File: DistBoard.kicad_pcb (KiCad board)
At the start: 2 copper layers, 63.6 x 50.8 mm, 21 parts, among them J1 22-27-2021, J2 SSM-103-L-SV, J3 SSM-103-L-SV, J4 SSM-103-L-SV, J5 SSM-103-L-SV, U1 TLE2426CDR

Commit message: Import board settings
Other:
- rule pad_to_mask_clearance: 0 -> 0.05
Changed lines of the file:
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@@
   (paper "A4")
   (layers
-    (0 "F.Cu" signal "Top Layer")
-    (31 "B.Cu" signal "Bottom Layer")
+    (0 "F.Cu" signal)
+    (31 "B.Cu" signal)
     (32 "B.Adhes" user "B.Adhesive")
     (33 "F.Adhes" user "F.Adhesive")
-    (34 "B.Paste" user "Bottom Paste")
-    (35 "F.Paste" user "Top Paste")
-    (36 "B.SilkS" user "Bottom Overlay")
-    (37 "F.SilkS" user "Top Overlay")
-    (38 "B.Mask" user "Bottom Solder")
-    (39 "F.Mask" user "Top Solder")
-    (40 "Dwgs.User" user "Mechanical 10")
+    (34 "B.Paste" user)
+    (35 "F.Paste" user)
+    (36 "B.SilkS" user "B.Silkscreen")
+    (37 "F.SilkS" user "F.Silkscreen")
+    (38 "B.Mask" user)
+    (39 "F.Mask" user)
+    (40 "Dwgs.User" user "User.Drawings")
     (41 "Cmts.User" user "User.Comments")
     (42 "Eco1.User" user "User.Eco1")
-    (43 "Eco2.User" user "Mechanical 11")
+    (43 "Eco2.User" user "User.Eco2")
     (44 "Edge.Cuts" user)
     (45 "Margin" user)
     (46 "B.CrtYd" user "B.Courtyard")
     (47 "F.CrtYd" user "F.Courtyard")
-    (48 "B.Fab" user "Mechanical 13")
-    (49 "F.Fab" user "Mechanical 12")
-    (50 "User.1" user "Mechanical 1")
-    (51 "User.2" user "Top 3D Body")
-    (52 "User.3" user "Bottom 3D Body")
-    (53 "User.4" user "Top Courtyard")
-    (54 "User.5" user "Bottom Courtyard")
-    (55 "User.6" user "Top Assembly")
-    (56 "User.7" user "Bottom Assembly")
-    (57 "User.8" user "Top Component Center")
-    (58 "User.9" user "Bottom Component Center")
+    (48 "B.Fab" user)
+    (49 "F.Fab" user)
+    (50 "User.1" user)
+    (51 "User.2" user)
+    (52 "User.3" user)
+    (53 "User.4" user)
+    (54 "User.5" user)
+    (55 "User.6" user)
+    (56 "User.7" user)
+    (57 "User.8" user)
+    (58 "User.9" user)
   )
   (setup
-    (pad_to_mask_clearance 0)
+    (stackup
+      (layer "F.SilkS" (type "Top Silk Screen"))
+      (layer "F.Paste" (type "Top Solder Paste"))
+      (layer "F.Mask" (type "Top Solder Mask") (thickness 0.01))
+      (layer "F.Cu" (type "copper") (thickness 0.035))
+      (layer "dielectric 1" (type "core") (thickness 1.51) (material "FR4") (epsilon_r 4.5) (loss_tangent 0.02))
+      (layer "B.Cu" (type "copper") (thickness 0.035))
+      (layer "B.Mask" (type "Bottom Solder Mask") (thickness 0.01))
+      (layer "B.Paste" (type "Bottom Solder Paste"))
+      (layer "B.SilkS" (type "Bottom Silk Screen"))
+      (copper_finish "None")
+      (dielectric_constraints no)
+    )
+    (pad_to_mask_clearance 0.05)
     (aux_axis_origin 116.6876 130.4036)
     (grid_origin 116.6876 130.4036)
@@
     )
   )
+  (property "SHEETTOTAL" "1")
   (net 0 "")
   (net 1 "NetF1_1")

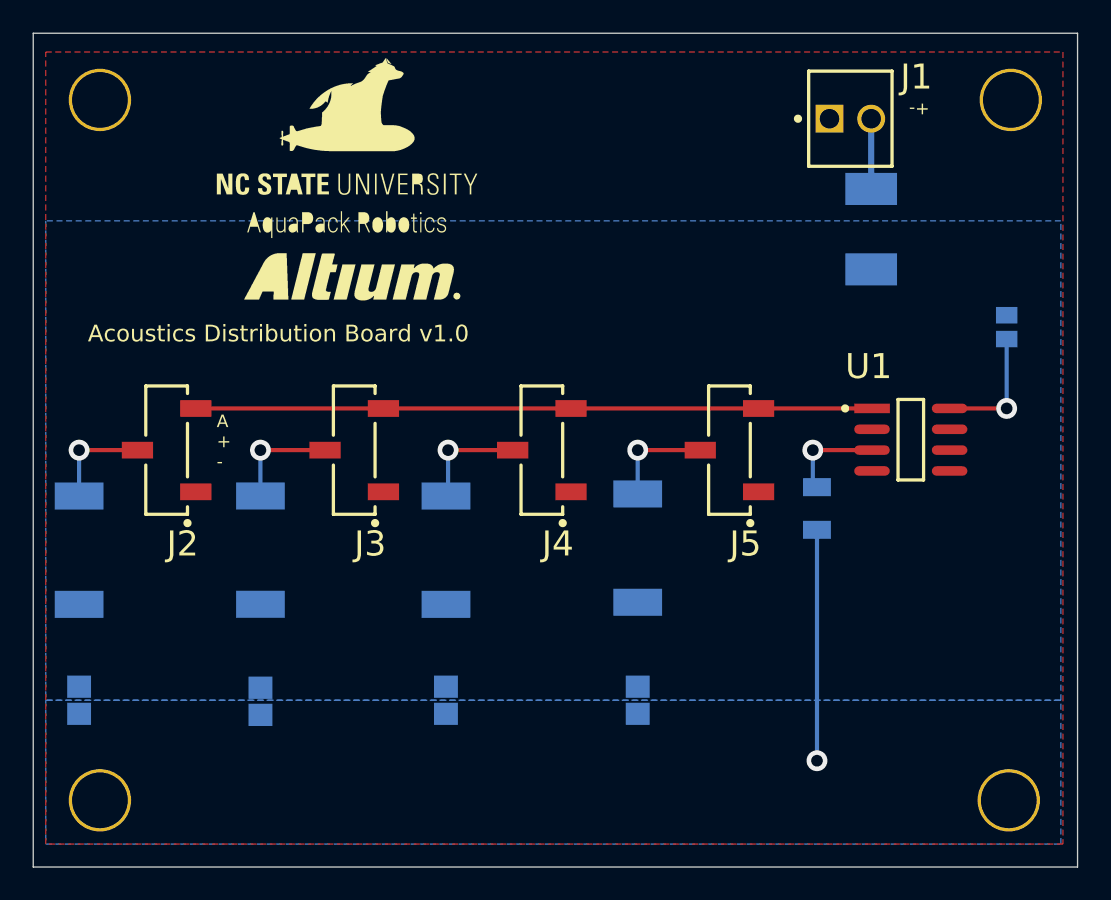
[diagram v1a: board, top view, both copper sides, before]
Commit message: Fix mounting holes
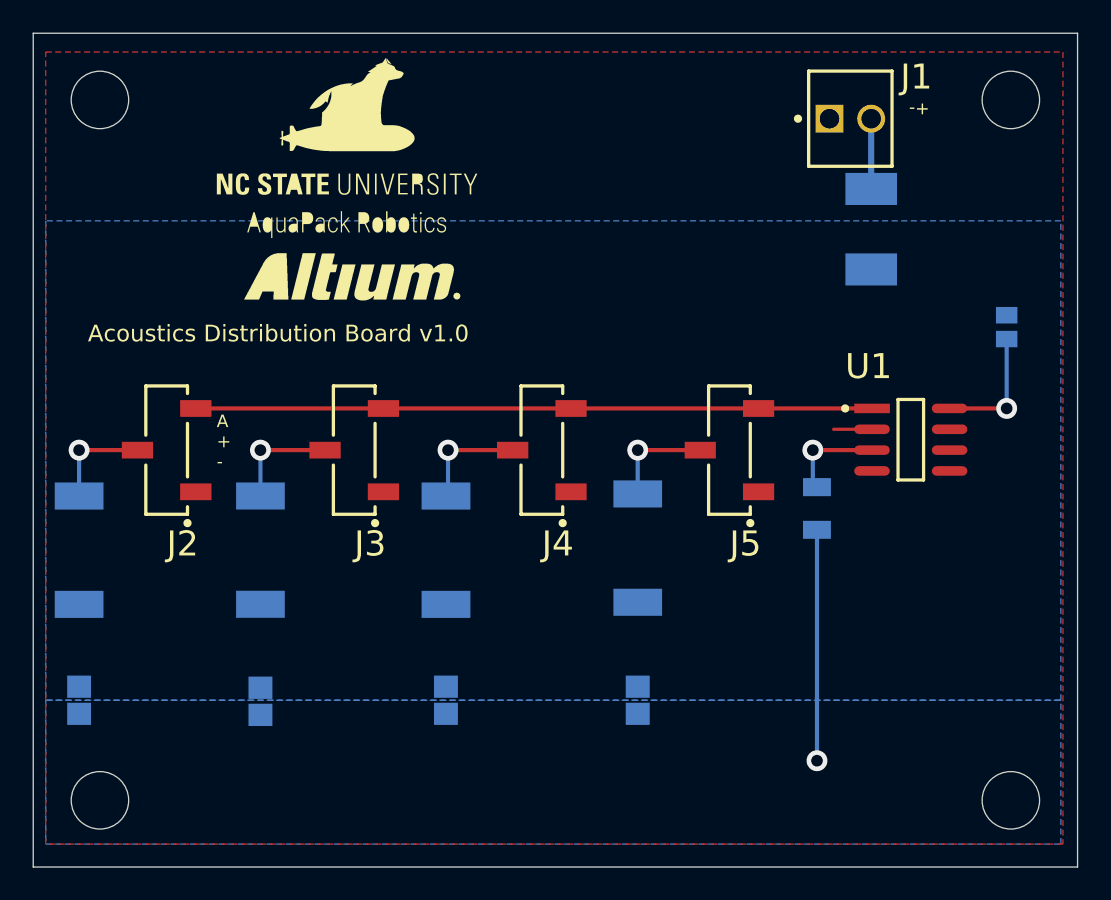
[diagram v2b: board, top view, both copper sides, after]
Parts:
- removed the ? at (120.8, 83.7)
- removed the ? at (120.8, 126.3)
- removed the ? at (176.1, 126.3)
- removed the ? at (176.3, 83.7)
- added ?: MountingHole_3.5mm, MountingHole:MountingHole_3.5mm, F.Cu at (176.3, 83.7)
- added ?: MountingHole_3.5mm, MountingHole:MountingHole_3.5mm, F.Cu at (176.3, 126.3)
- added ?: MountingHole_3.5mm, MountingHole:MountingHole_3.5mm, F.Cu at (120.8, 83.7)
- added ?: MountingHole_3.5mm, MountingHole:MountingHole_3.5mm, F.Cu at (120.8, 126.3)
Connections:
- net AGND renamed /AGND
- net NR renamed /NR
- net NetF1_1 renamed Net-(F1-Pad1)
- net NetF2_2 renamed Net-(F2-Pad2)
- net NetF3_2 renamed Net-(F3-Pad2)
- net NetF4_2 renamed Net-(F4-Pad2)
- net NetF5_2 renamed Net-(F5-Pad2)
- net VCC renamed /VCC
- U1 pad 4: (no net) -> unconnected-(U1-NC-Pad4)
- U1 pad 5: (no net) -> unconnected-(U1-NC-Pad5)
- U1 pad 6: (no net) -> unconnected-(U1-NC-Pad6)
- U1 pad 7: (no net) -> unconnected-(U1-NC-Pad7)
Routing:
- net GND: track 14.3 -> 16.7 mm

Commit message: Fix silkscreen sizes
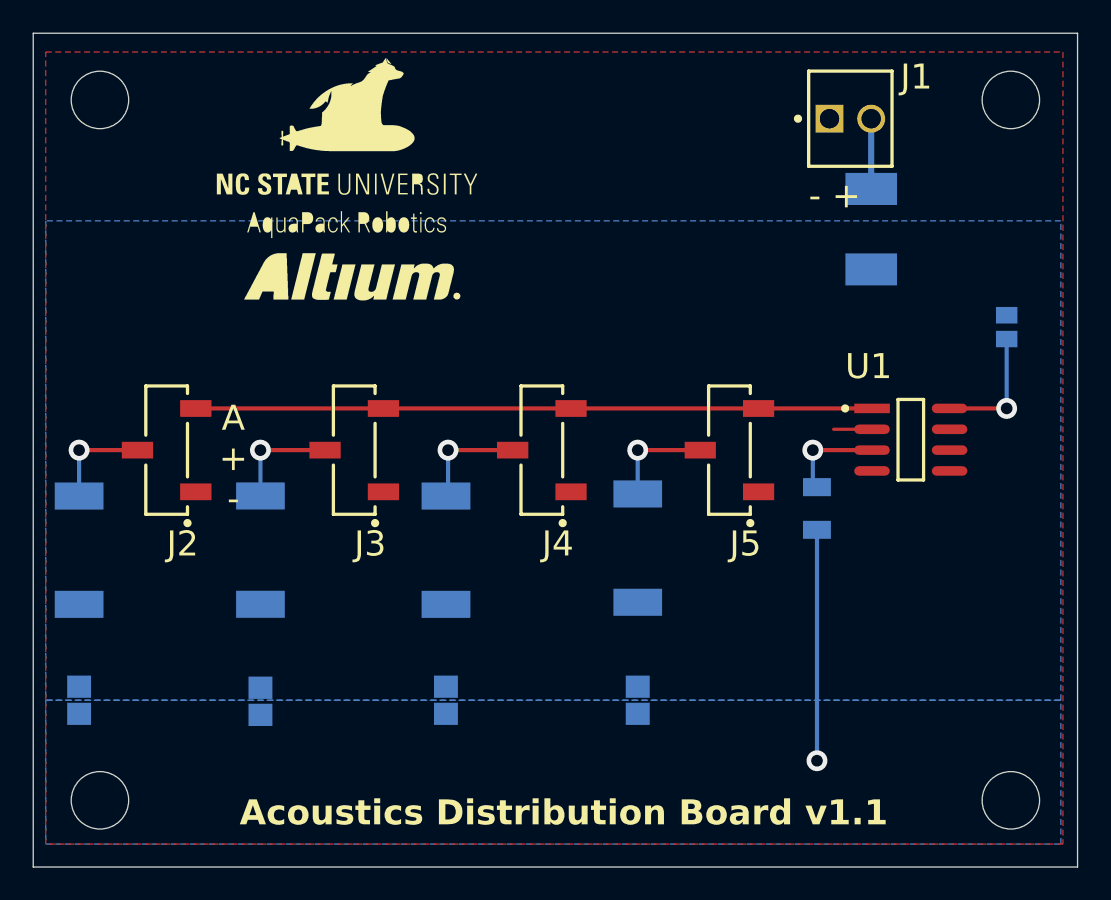
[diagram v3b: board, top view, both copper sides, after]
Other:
- board text added: "- +"
- board text added: "Acoustics Distribution Board v1.1"
- board text removed: "+-"
- board text removed: "Acoustics Distribution Board v1.0"
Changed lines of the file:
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@@
     (property "WEIGHT" "0.000335oz")
     (property "WIDTH" "0.049inch")
-    (fp_text reference "C5" (at 1.77825 1.14259 180 unlocked) (layer "B.SilkS")
+    (fp_text reference "C5" (at 4.191 -1.651 180 unlocked) (layer "B.SilkS")
         (effects (font (size 1.524 1.524) (thickness 0.254)) (justify left bottom mirror))
     )
@@
   (gr_line (start 116.6876 79.6036) (end 180.3146 79.6036)
     (stroke (width 0.254) (type solid)) (layer "User.1"))
-  (gr_text "+-" (at 171.2976 83.79464 180) (layer "F.SilkS")
-    (effects (font (size 0.762 0.762) (thickness 0.127)) (justify left bottom))
+  (gr_text "A\n+\n-" (at 128.8796 105.5116) (layer "F.SilkS")
+    (effects (font (size 1.524 1.524) (thickness 0.2032)))
   )
-  (gr_text "A\n+\n-" (at 127.8636 106.1466) (layer "F.SilkS")
-    (effects (font (size 0.762 0.762) (thickness 0.127)) (justify left bottom))
+  (gr_text "Acoustics Distribution Board v1.1" (at 129.2606 127.9906) (layer "F.SilkS")
+    (effects (font (size 1.524 1.524) (thickness 0.2032) bold) (justify left bottom))
   )
-  (gr_text "Acoustics Distribution Board v1.0" (at 120.015 98.5012) (layer "F.SilkS")
-    (effects (font (size 1.016 1.016) (thickness 0.1524)) (justify left bottom))
+  (gr_text "- +" (at 163.9316 90.3986) (layer "F.SilkS")
+    (effects (font (size 1.524 1.524) (thickness 0.2032)) (justify left bottom))
   )
   (dimension (type aligned) (layer "User.1")

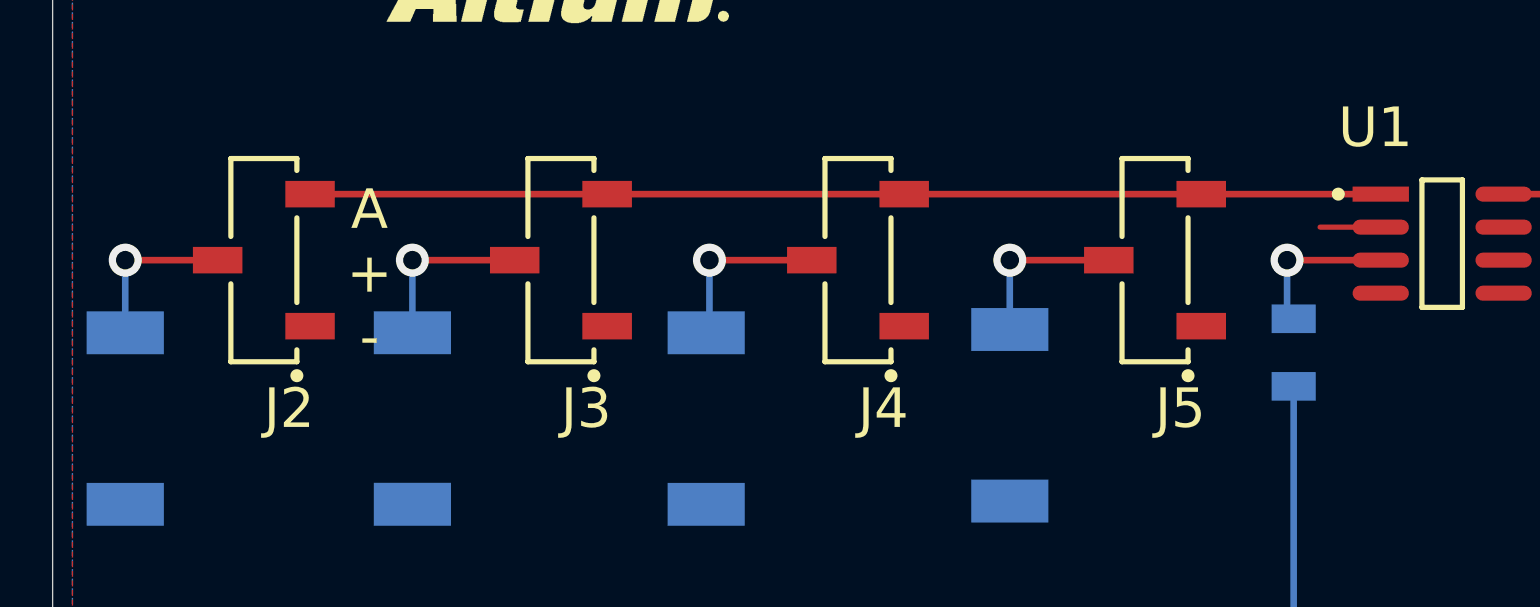
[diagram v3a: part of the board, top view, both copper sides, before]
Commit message: Swap to through hole headers
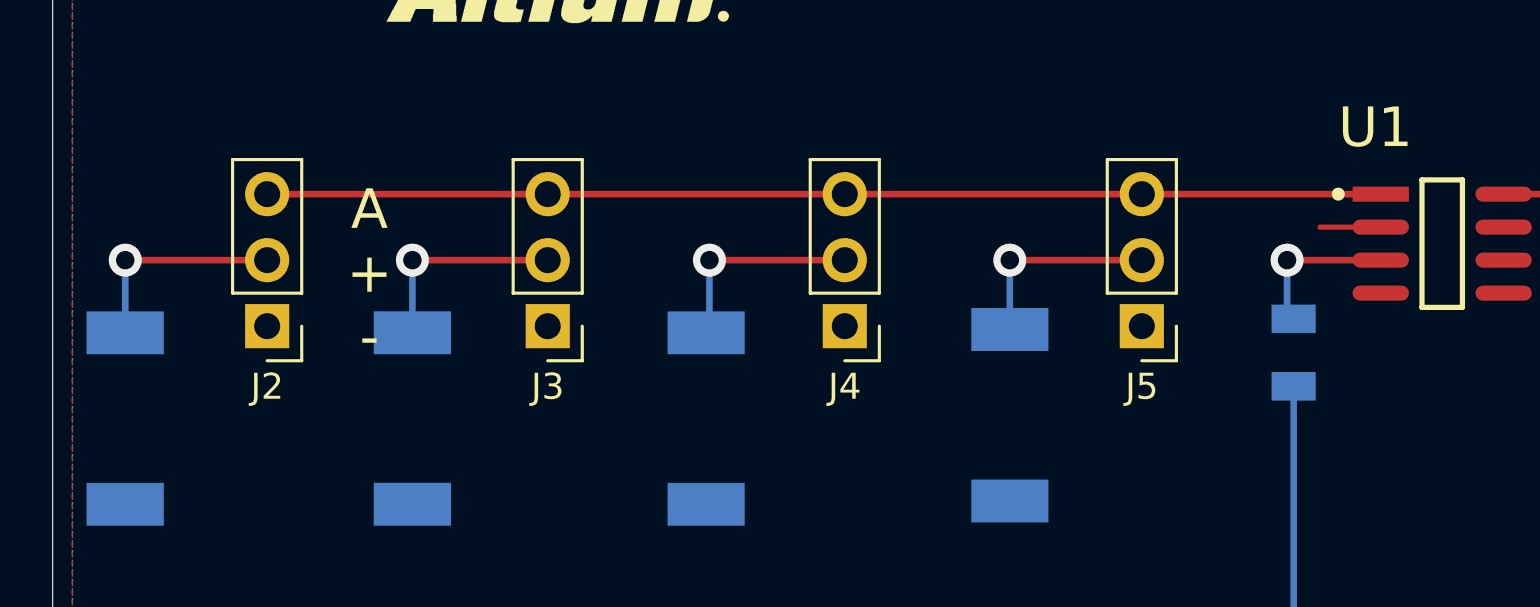
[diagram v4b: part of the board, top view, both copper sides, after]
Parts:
- J2, J3, J4, J5: value SSM-103-L-SV -> Conn_01x03; footprint AltiumImport:SMTC-SSM-103-X-SV -> Connector_PinHeader_2.54mm:PinHeader_1x03_P2.54mm_Vertical
- moved J3 2.59 mm to (135.7, 107.5), turned to 180 degrees
- moved J4 2.59 mm to (147.2, 107.5), turned to 180 degrees
- moved J5 2.59 mm to (158.6, 107.5), turned to 180 degrees
- moved J2 2.54 mm to (124.9, 107.5), turned to 180 degrees
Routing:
- net Net-(J2-Pin_2): track 6.35 -> 8.26 mm
- net /AGND: track 41.2 -> 42.8 mm
- net Net-(J5-Pin_2): track 6.48 -> 7.75 mm
- net Net-(J3-Pin_2): track 6.73 -> 8.00 mm
- net Net-(J4-Pin_2): track 6.79 -> 8.06 mm
